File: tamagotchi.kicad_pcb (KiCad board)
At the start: 2 copper layers, 60.8 x 77.1 mm, 9 parts, among them SW1 SW_Push, SW2 SW_Push, SW3 SW_Push, U1 XIAO-ESP32-C3-SMD, U2 HS96L03W2C03

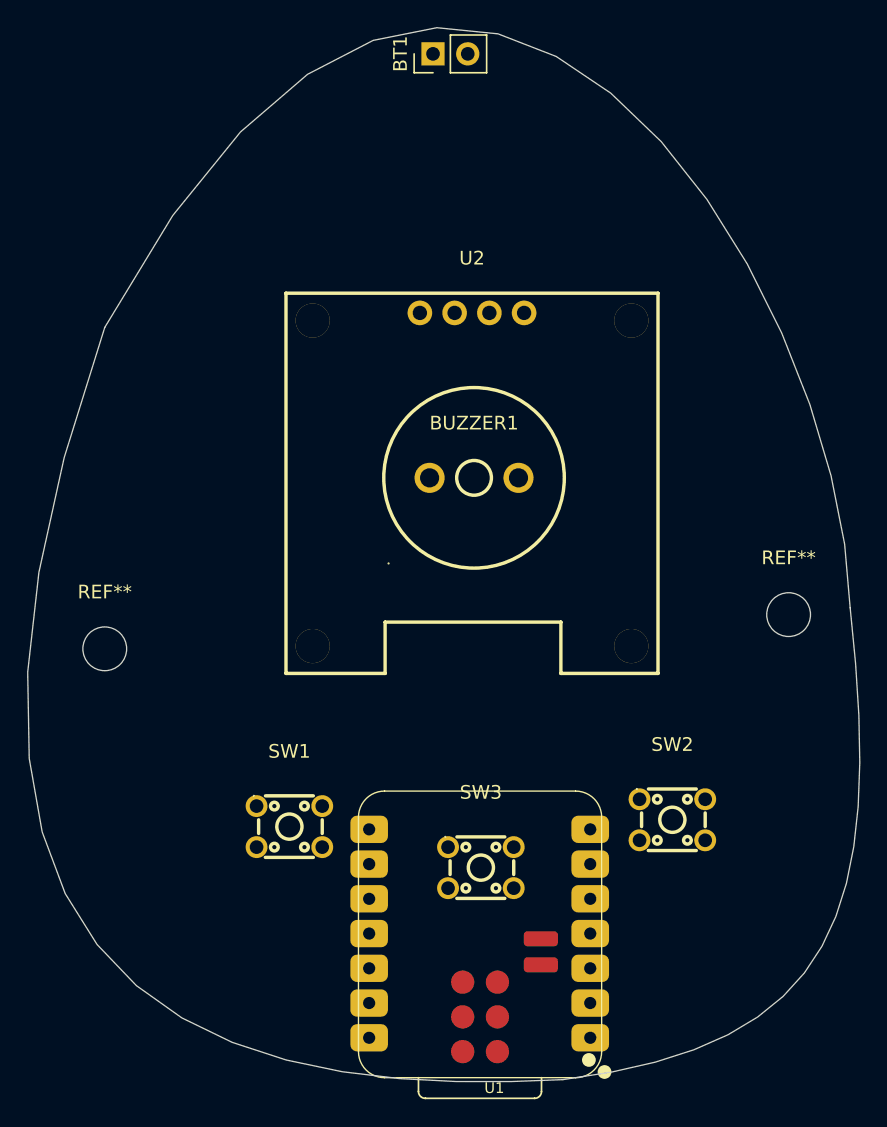
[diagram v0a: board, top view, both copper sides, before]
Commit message: added some routing and furby art
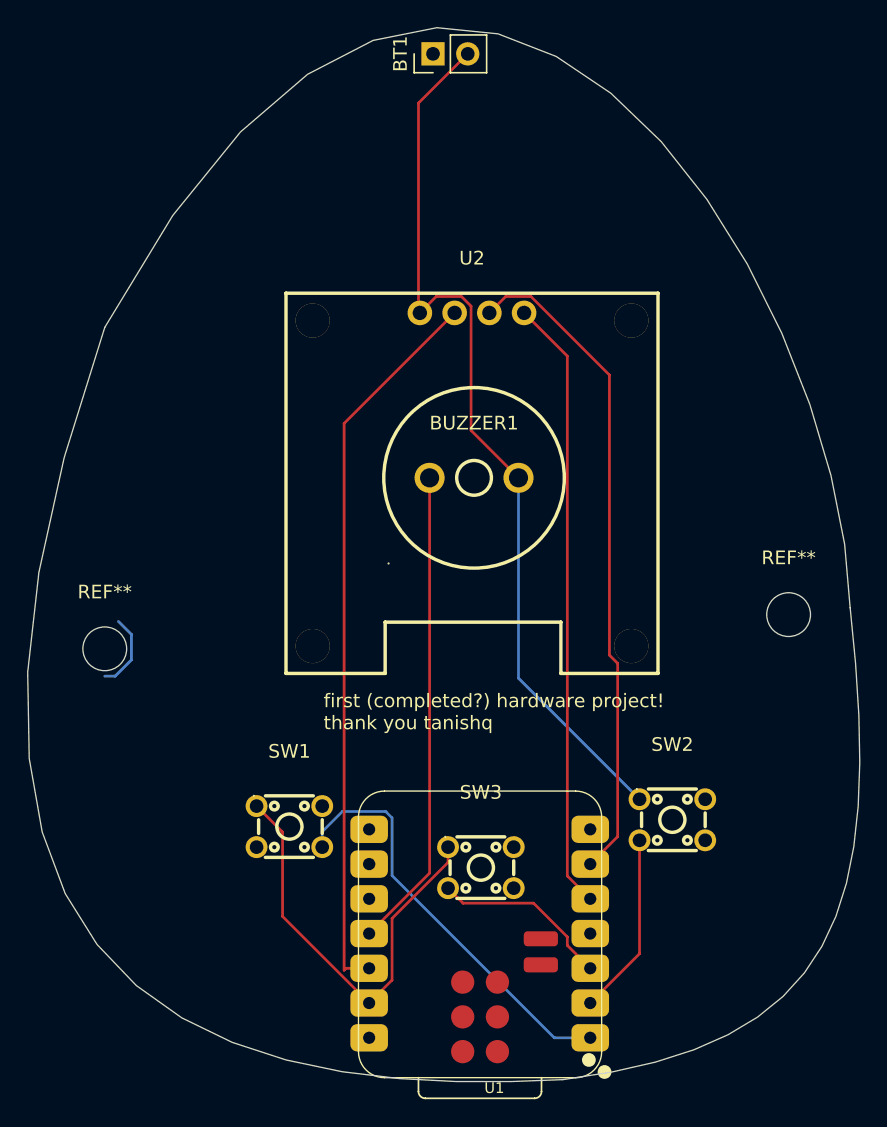
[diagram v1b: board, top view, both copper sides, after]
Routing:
- net GND: track 0.00 -> 97.8 mm
- net +3V3: track 0.00 -> 53.3 mm
- net Net-(U1-GPIO7_D5_SCL): track 0.00 -> 48.5 mm
- net Net-(U1-GPIO6_D4_SDA): track 0.00 -> 44.8 mm
- net Net-(BUZZER1-+): track 0.00 -> 35.2 mm
- net Net-(U1-GPIO2_A0_D0): track 0.00 -> 30.7 mm
- net Net-(U1-GPIO3_A1_D1): track 0.00 -> 13.4 mm
- net Net-(U1-GPIO4_A2_D2): track 0.00 -> 13.2 mm
- net (no net): track 0.00 -> 5.65 mm
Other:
- board text added: "first (completed?) hardware project! thank you tanishq"
- board text added: "tamagotchi <3"
